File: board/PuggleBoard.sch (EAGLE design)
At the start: 129 parts, among them U1 OPA4209, U10 24C, U2 ADS8331, U3 AD5686, U4 OPA4209, U5 LM2663, U6 TPS7A3001, U7 TPS7A4901, U8 REF5040, U9 AD8032

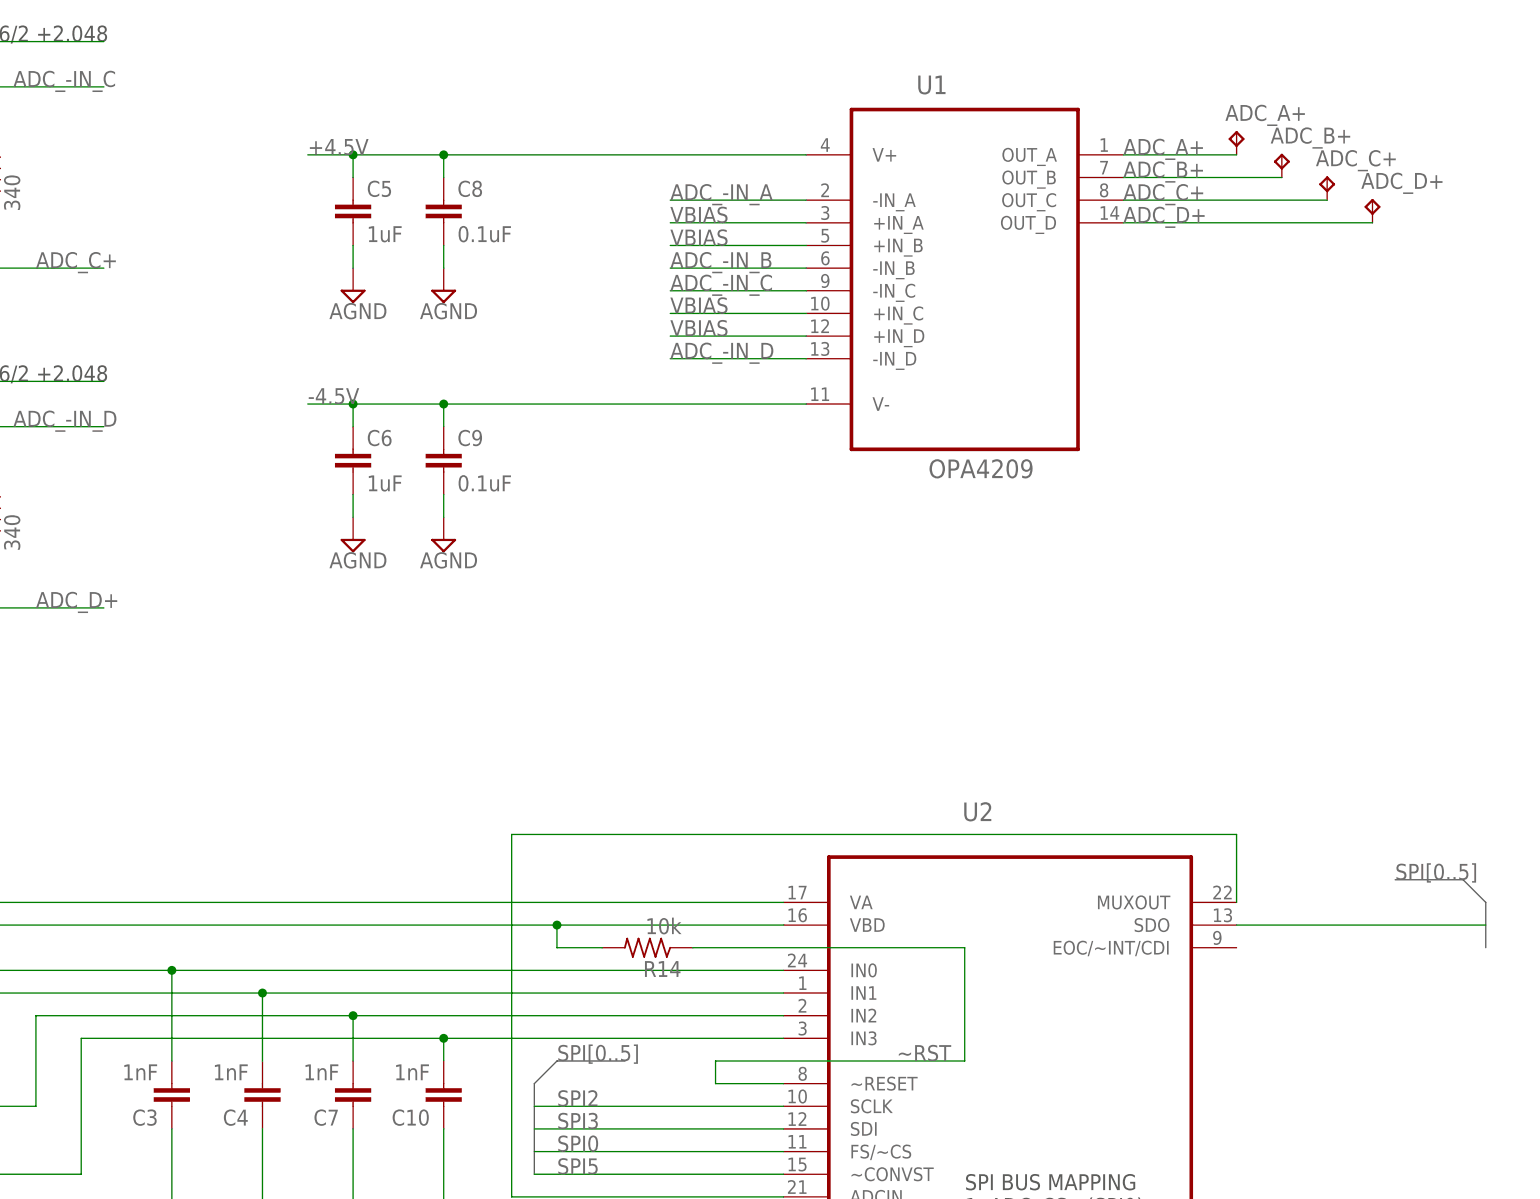
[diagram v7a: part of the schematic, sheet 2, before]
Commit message: Laying out relative positions of functional modules (e.g power, regulation, buffer, conversion, etc).
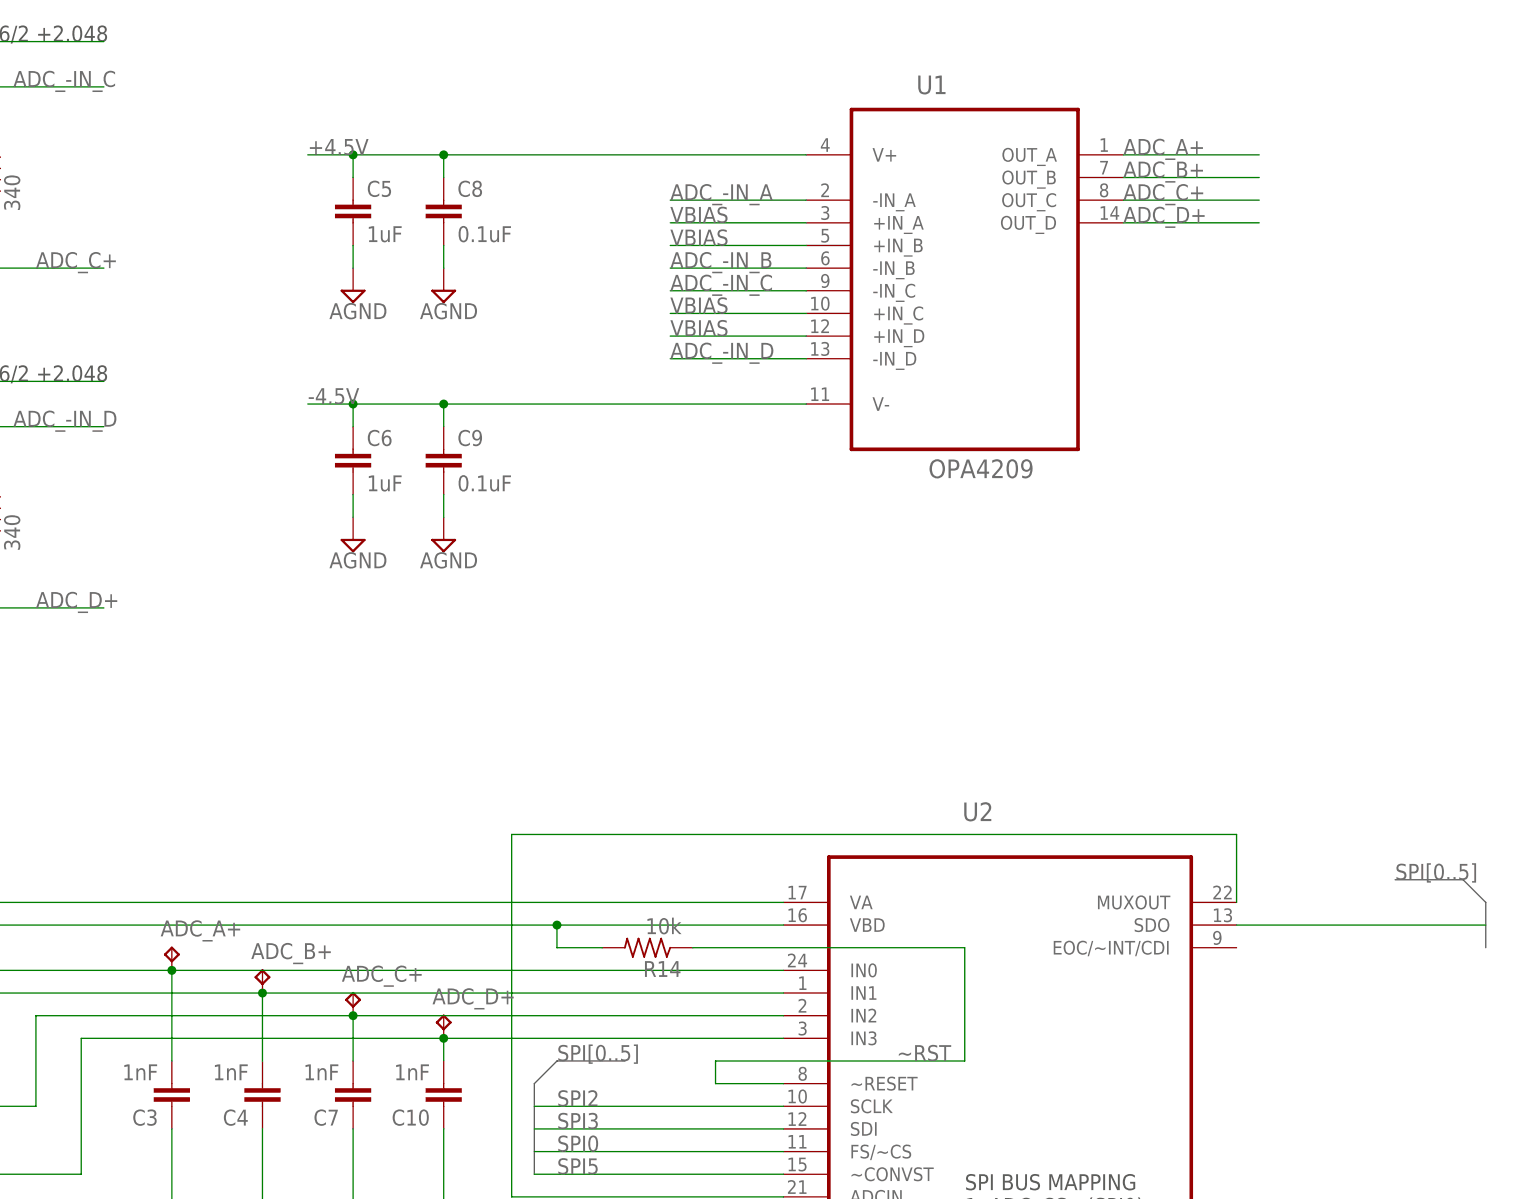
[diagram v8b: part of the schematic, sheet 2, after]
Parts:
- EEPROM_WP: value TPB1,27 -> TPTP14SQ; device testpad:TPB1,27 -> testpad:TPTP14SQ
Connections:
- removed net N$6: A_I/O.3
- removed net N$8: A_I/O.9
- net ADC_A+: no longer ADC_A+.TP
- net ADC_B+: no longer ADC_B+.TP
- net ADC_C+: no longer ADC_C+.TP
- net ADC_D+: no longer ADC_D+.TP
- net DAC_A: now also A_I/O.3
- net DAC_D: now also A_I/O.9
- net N$40: now also ADC_A+.TP
- net N$41: now also ADC_B+.TP
- net N$42: now also ADC_C+.TP
- net N$43: now also ADC_D+.TP
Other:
- moved on the sheet: ADC_A+, ADC_B+, ADC_C+, ADC_D+
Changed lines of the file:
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@@
 <part name="R24" library="rcl" deviceset="R-US_" device="R0603" value="680"/>
 <part name="S1" library="smd-special" deviceset="SWS002" device=""/>
-<part name="EEPROM_WP" library="testpad" deviceset="TP" device="B1,27"/>
+<part name="EEPROM_WP" library="testpad" deviceset="TP" device="TP14SQ" value="TPTP14SQ"/>
 <part name="SUPPLY9" library="supply2" deviceset="AGND" device=""/>
 <part name="GND1" library="supply1" deviceset="GND" device="" value="PGND"/>
@@
 </segment>
 </net>
-<net name="N$6" class="0">
+<net name="DAC_A" class="0">
 <segment>
 <pinref part="A_I/O" gate="G$1" pin="3"/>
@@
 </segment>
 </net>
-<net name="N$8" class="0">
+<net name="DAC_D" class="0">
 <segment>
 <pinref part="A_I/O" gate="G$1" pin="9"/>
@@
 <instance part="SUPPLY18" gate="G$1" x="12.7" y="165.1"/>
 <instance part="R14" gate="G$1" x="35.56" y="91.44" rot="R180"/>
-<instance part="ADC_A+" gate="G$1" x="101.6" y="182.88"/>
+<instance part="ADC_A+" gate="G$1" x="-17.78" y="91.44"/>
 <instance part="R13" gate="G$1" x="17.78" y="55.88" rot="R180"/>
 <instance part="U1" gate="A" x="71.12" y="170.18"/>
@@
 <instance part="SUPPLY41" gate="G$1" x="2.54" y="165.1"/>
 <instance part="SUPPLY42" gate="G$1" x="2.54" y="137.16"/>
-<instance part="ADC_B+" gate="G$1" x="106.68" y="180.34"/>
-<instance part="ADC_C+" gate="G$1" x="111.76" y="177.8"/>
-<instance part="ADC_D+" gate="G$1" x="116.84" y="175.26"/>
+<instance part="ADC_B+" gate="G$1" x="-7.62" y="88.9"/>
+<instance part="ADC_C+" gate="G$1" x="2.54" y="86.36"/>
+<instance part="ADC_D+" gate="G$1" x="12.7" y="83.82"/>
 <instance part="R1" gate="G$1" x="-106.68" y="149.86" rot="R180"/>
 <instance part="R3" gate="G$1" x="-96.52" y="139.7" rot="R90"/>
@@
 <segment>
 <pinref part="U1" gate="A" pin="OUT_B"/>
-<wire x1="88.9" y1="177.8" x2="106.68" y2="177.8" width="0.1524" layer="91"/>
 <label x="88.9" y="177.8" size="1.778" layer="95"/>
-<pinref part="ADC_B+" gate="G$1" pin="TP"/>
+<wire x1="88.9" y1="177.8" x2="104.14" y2="177.8" width="0.1524" layer="91"/>
 </segment>
 <segment>
@@
 <wire x1="-17.78" y1="78.74" x2="-17.78" y2="88.9" width="0.1524" layer="91"/>
 <junction x="-17.78" y="88.9"/>
+<pinref part="ADC_A+" gate="G$1" pin="TP"/>
 </segment>
 </net>
@@
 <wire x1="-7.62" y1="78.74" x2="-7.62" y2="86.36" width="0.1524" layer="91"/>
 <junction x="-7.62" y="86.36"/>
+<pinref part="ADC_B+" gate="G$1" pin="TP"/>
 </segment>
 </net>
@@
 <wire x1="2.54" y1="78.74" x2="2.54" y2="83.82" width="0.1524" layer="91"/>
 <junction x="2.54" y="83.82"/>
+<pinref part="ADC_C+" gate="G$1" pin="TP"/>
 </segment>
 </net>
@@
 <wire x1="12.7" y1="78.74" x2="12.7" y2="81.28" width="0.1524" layer="91"/>
 <junction x="12.7" y="81.28"/>
+<pinref part="ADC_D+" gate="G$1" pin="TP"/>
 </segment>
 </net>
@@
 <segment>
 <pinref part="U1" gate="A" pin="OUT_A"/>
-<wire x1="88.9" y1="180.34" x2="101.6" y2="180.34" width="0.1524" layer="91"/>
-<pinref part="ADC_A+" gate="G$1" pin="TP"/>
 <label x="88.9" y="180.34" size="1.778" layer="95"/>
+<wire x1="88.9" y1="180.34" x2="104.14" y2="180.34" width="0.1524" layer="91"/>
 </segment>
 </net>
@@
 <segment>
 <pinref part="U1" gate="A" pin="OUT_C"/>
-<wire x1="88.9" y1="175.26" x2="111.76" y2="175.26" width="0.1524" layer="91"/>
 <label x="88.9" y="175.26" size="1.778" layer="95"/>
-<pinref part="ADC_C+" gate="G$1" pin="TP"/>
+<wire x1="88.9" y1="175.26" x2="104.14" y2="175.26" width="0.1524" layer="91"/>
 </segment>
 <segment>
@@
 <pinref part="U1" gate="A" pin="OUT_D"/>
 <label x="88.9" y="172.72" size="1.778" layer="95"/>
-<pinref part="ADC_D+" gate="G$1" pin="TP"/>
-<wire x1="88.9" y1="172.72" x2="116.84" y2="172.72" width="0.1524" layer="91"/>
-</segment>
-<segment>
+<wire x1="88.9" y1="172.72" x2="104.14" y2="172.72" width="0.1524" layer="91"/>
+</segment>
+<segment>
